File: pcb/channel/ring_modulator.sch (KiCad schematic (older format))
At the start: 15 parts, among them IC9 MCP6074-E_ST

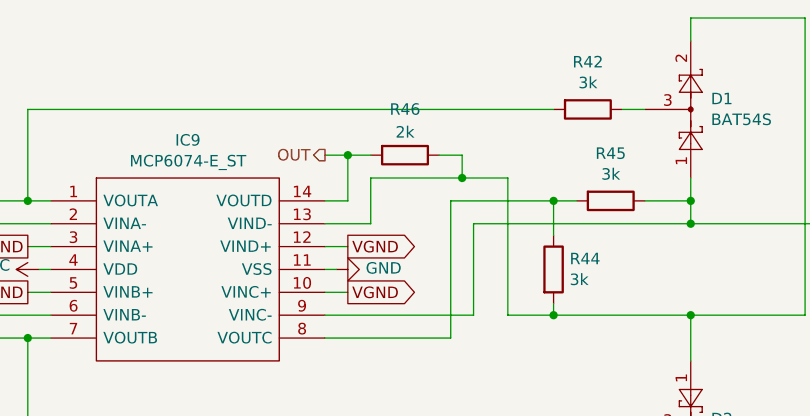
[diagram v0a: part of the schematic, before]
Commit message: Increase ring modulator gain for 100mVpp output
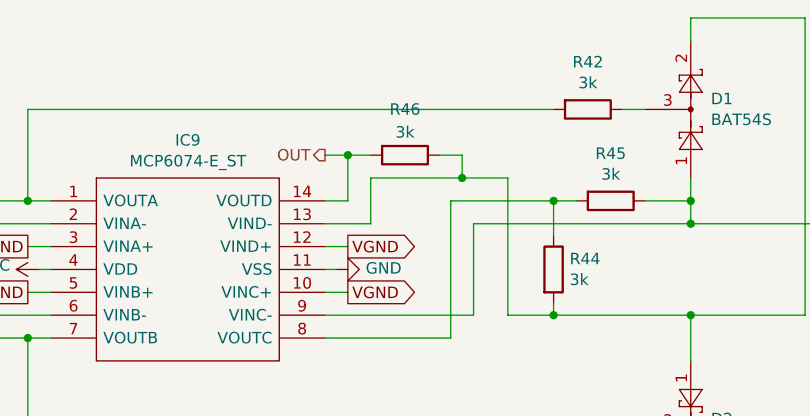
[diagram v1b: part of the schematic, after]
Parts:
- R46: value 2k -> 3k
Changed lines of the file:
@@
 P 6650 3850
 F 0 "R46" V 6450 3850 50  0000 C CNN
-F 1 "2k" V 6550 3850 50  0000 C CNN
+F 1 "3k" V 6550 3850 50  0000 C CNN
 F 2 "Resistor_SMD:R_0603_1608Metric_Pad1.05x0.95mm_HandSolder" V 6580 3850 50  0001 C CNN
 F 3 "~" H 6650 3850 50  0001 C CNN
